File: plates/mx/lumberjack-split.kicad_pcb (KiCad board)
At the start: 2 copper layers, 114.3 x 95.3 mm, 0 parts

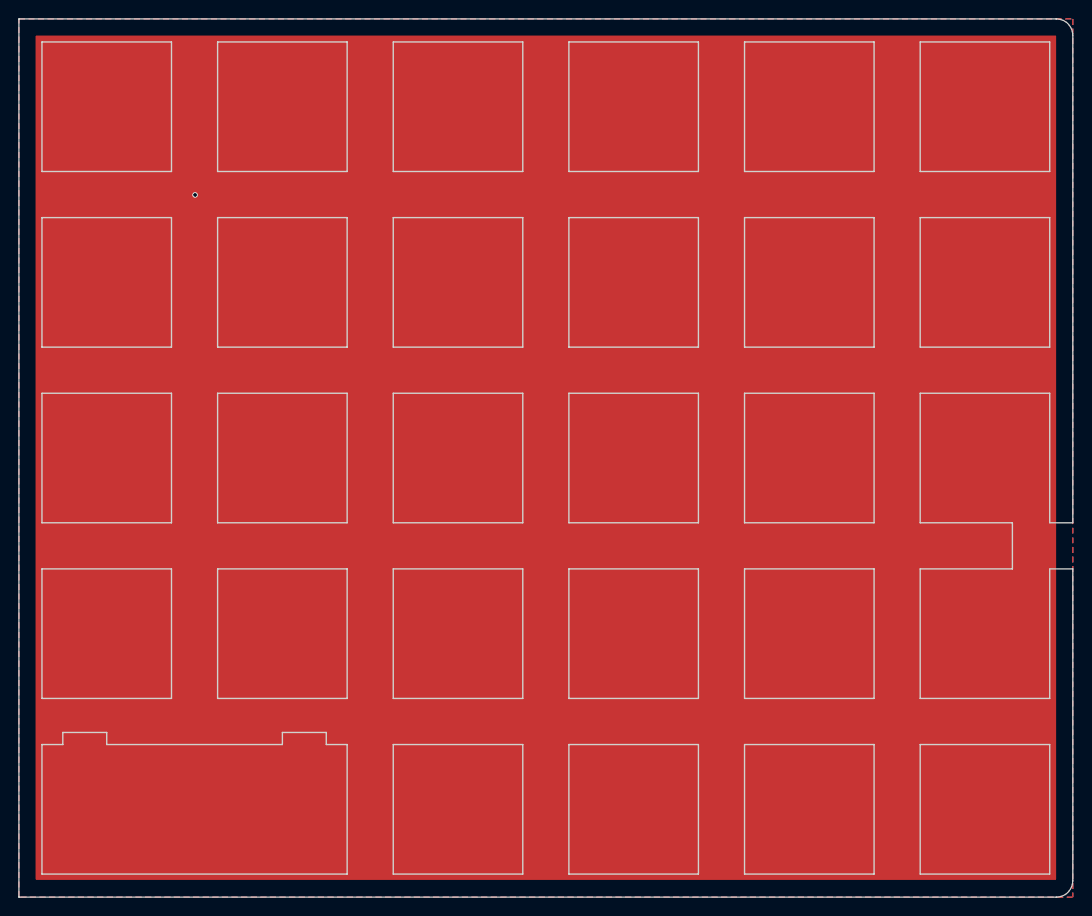
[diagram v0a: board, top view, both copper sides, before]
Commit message: Fix copper outline missing on the back side of MX split plates
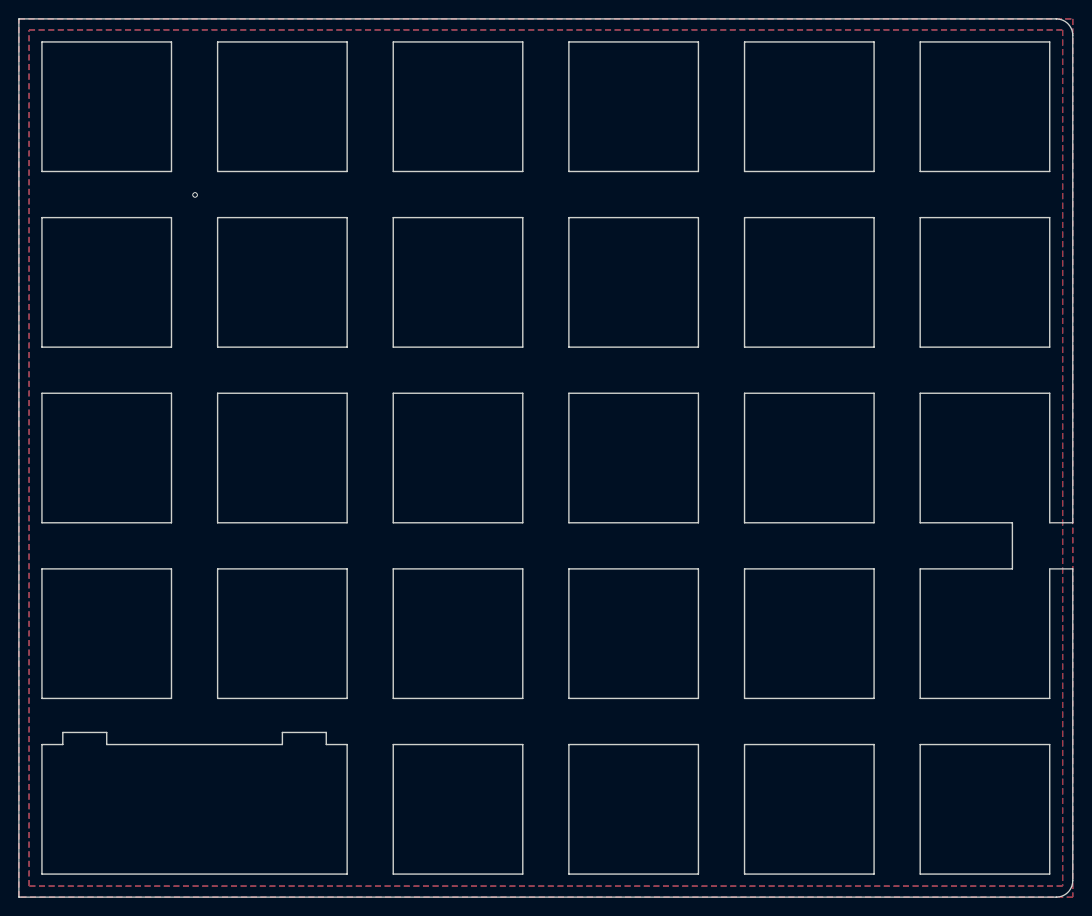
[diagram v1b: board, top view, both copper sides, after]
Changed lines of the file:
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@@
       (drillshape 0)
       (scaleselection 1)
-      (outputdirectory "gerbers")
+      (outputdirectory "../gerbers")
     )
   )
   (net 0 "")
-  (gr_rect (start 214.789652 143.29232) (end 104.299188 51.911468) (layer "F.Cu") (width 0.2) (fill solid))
+  (gr_rect (start 123.349188 51.911468) (end 138.589188 67.151468) (layer "B.Mask") (width 0.1) (fill solid))
+  (gr_rect (start 161.449188 109.061468) (end 176.689188 124.301468) (layer "B.Mask") (width 0.1) (fill solid))
+  (gr_rect (start 180.499188 70.961468) (end 195.739188 86.201468) (layer "B.Mask") (width 0.1) (fill solid))
+  (gr_rect (start 161.449188 51.911468) (end 176.689188 67.151468) (layer "B.Mask") (width 0.1) (fill solid))
+  (gr_rect (start 199.549188 51.911468) (end 214.789188 67.151468) (layer "B.Mask") (width 0.1) (fill solid))
+  (gr_rect (start 180.499188 109.061468) (end 195.739188 124.301468) (layer "B.Mask") (width 0.1) (fill solid))
+  (gr_rect (start 161.449188 70.961468) (end 176.689188 86.201468) (layer "B.Mask") (width 0.1) (fill solid))
+  (gr_rect (start 142.399188 109.061468) (end 157.639188 124.301468) (layer "B.Mask") (width 0.1) (fill solid))
+  (gr_rect (start 142.399188 128.111468) (end 157.639188 143.351468) (layer "B.Mask") (width 0.1) (fill solid))
+  (gr_rect (start 199.549188 109.061468) (end 214.789188 124.301468) (layer "B.Mask") (width 0.1) (fill solid))
+  (gr_rect (start 180.499188 90.011468) (end 195.739188 105.251468) (layer "B.Mask") (width 0.1) (fill solid))
+  (gr_rect (start 199.549188 70.961468) (end 214.789188 86.201468) (layer "B.Mask") (width 0.1) (fill solid))
+  (gr_rect (start 104.299188 70.961468) (end 119.539188 86.201468) (layer "B.Mask") (width 0.1) (fill solid))
+  (gr_rect (start 123.349188 109.061468) (end 138.589188 124.301468) (layer "B.Mask") (width 0.1) (fill solid))
+  (gr_rect (start 180.499188 51.911468) (end 195.739188 67.151468) (layer "B.Mask") (width 0.1) (fill solid))
+  (gr_rect (start 104.299188 109.061468) (end 119.539188 124.301468) (layer "B.Mask") (width 0.1) (fill solid))
+  (gr_rect (start 104.299188 90.011468) (end 119.539188 105.251468) (layer "B.Mask") (width 0.1) (fill solid))
+  (gr_rect (start 123.349188 70.961468) (end 138.589188 86.201468) (layer "B.Mask") (width 0.1) (fill solid))
+  (gr_rect (start 199.549188 128.111468) (end 214.789188 143.351468) (layer "B.Mask") (width 0.1) (fill solid))
+  (gr_rect (start 142.399188 90.011468) (end 157.639188 105.251468) (layer "B.Mask") (width 0.1) (fill solid))
+  (gr_rect (start 123.349188 90.011468) (end 138.589188 105.251468) (layer "B.Mask") (width 0.1) (fill solid))
+  (gr_rect (start 142.399188 70.961468) (end 157.639188 86.201468) (layer "B.Mask") (width 0.1) (fill solid))
+  (gr_rect (start 104.299188 51.911468) (end 119.539188 67.151468) (layer "B.Mask") (width 0.1) (fill solid))
+  (gr_rect (start 104.299188 128.111468) (end 138.589268 143.351468) (layer "B.Mask") (width 0.1) (fill solid))
+  (gr_rect (start 161.449188 128.111468) (end 176.689188 143.351468) (layer "B.Mask") (width 0.1) (fill solid))
+  (gr_rect (start 199.549188 90.011468) (end 214.789188 105.251468) (layer "B.Mask") (width 0.1) (fill solid))
+  (gr_rect (start 180.499188 128.111468) (end 195.739188 143.351468) (layer "B.Mask") (width 0.1) (fill solid))
+  (gr_rect (start 142.399188 51.911468) (end 157.639188 67.151468) (layer "B.Mask") (width 0.1) (fill solid))
+  (gr_rect (start 161.449188 90.011468) (end 176.689188 105.251468) (layer "B.Mask") (width 0.1) (fill solid))
   (gr_rect (start 161.449524 51.911436) (end 176.689524 67.151436) (layer "F.Mask") (width 0.1) (fill solid))
   (gr_rect (start 123.3493 90.011564) (end 138.5893 105.251564) (layer "F.Mask") (width 0.1) (fill solid))
@@
   (gr_line (start 195.144198 71.556922) (end 195.144198 85.606297) (layer "Edge.Cuts") (width 0.15))
   (via (at 121.5 69.1) (size 0.6) (drill 0.4) (layers "F.Cu" "B.Cu") (net 0))
-  (zone (net 0) (net_name "") (layer "F.Cu") (hatch edge 0.508)
+  (zone (net 0) (net_name "") (layers F&B.Cu) (hatch edge 0.508)
     (connect_pads (clearance 0.508))
     (min_thickness 0.254) (filled_areas_thickness no)
@@
     )
   )
-  (zone (net 0) (net_name "") (layer "B.Cu") (hatch edge 0.508)
-    (connect_pads (clearance 0.508))
+  (zone (net 0) (net_name "") (layers F&B.Cu) (hatch edge 0.508)
+    (connect_pads (clearance 0))
     (min_thickness 0.254) (filled_areas_thickness no)
     (fill yes (thermal_gap 0.508) (thermal_bridge_width 0.508))
     (polygon
       (pts
-        (xy 216.693932 145.256372)
-        (xy 102.393836 145.256372)
-        (xy 102.393836 50.006292)
-        (xy 216.693932 50.006292)
+        (xy 215.593932 144.056372)
+        (xy 103.493836 144.056372)
+        (xy 103.493836 51.206292)
+        (xy 215.593932 51.206292)
       )
     )
